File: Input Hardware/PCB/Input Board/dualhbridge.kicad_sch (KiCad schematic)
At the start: 2 parts, among them U1 DRV8837

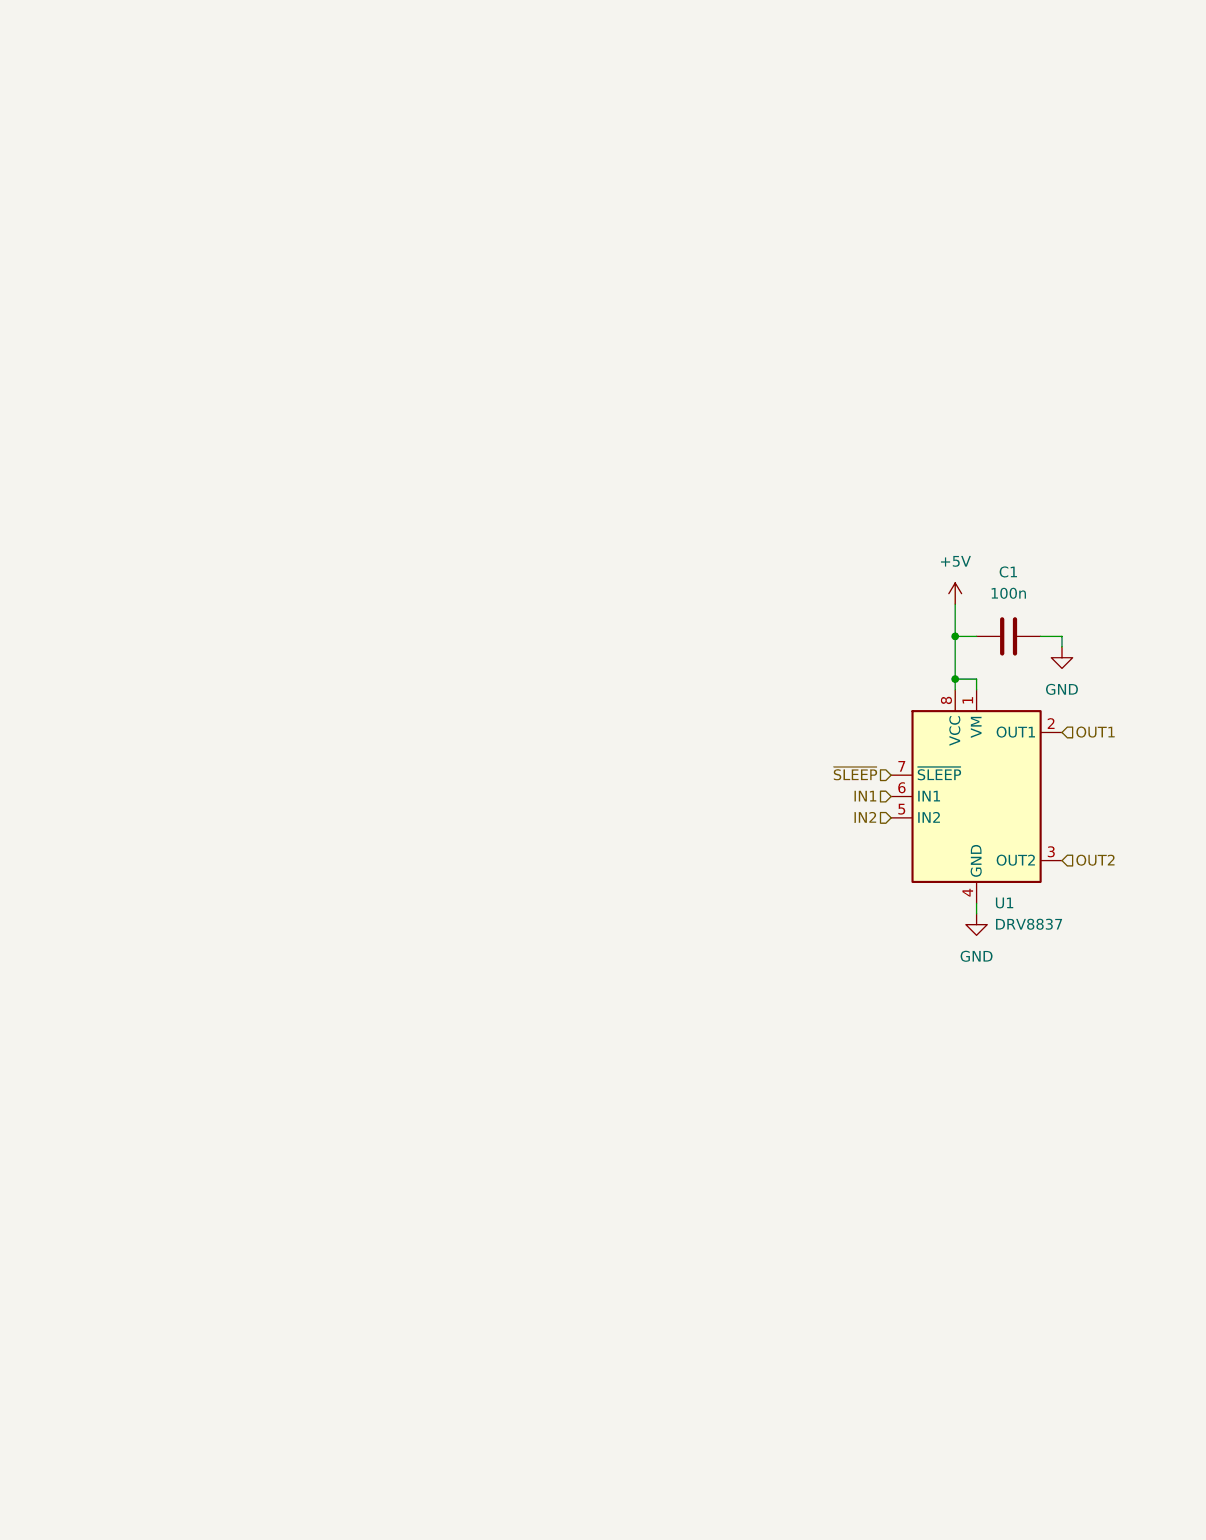
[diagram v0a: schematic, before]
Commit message: driver format update
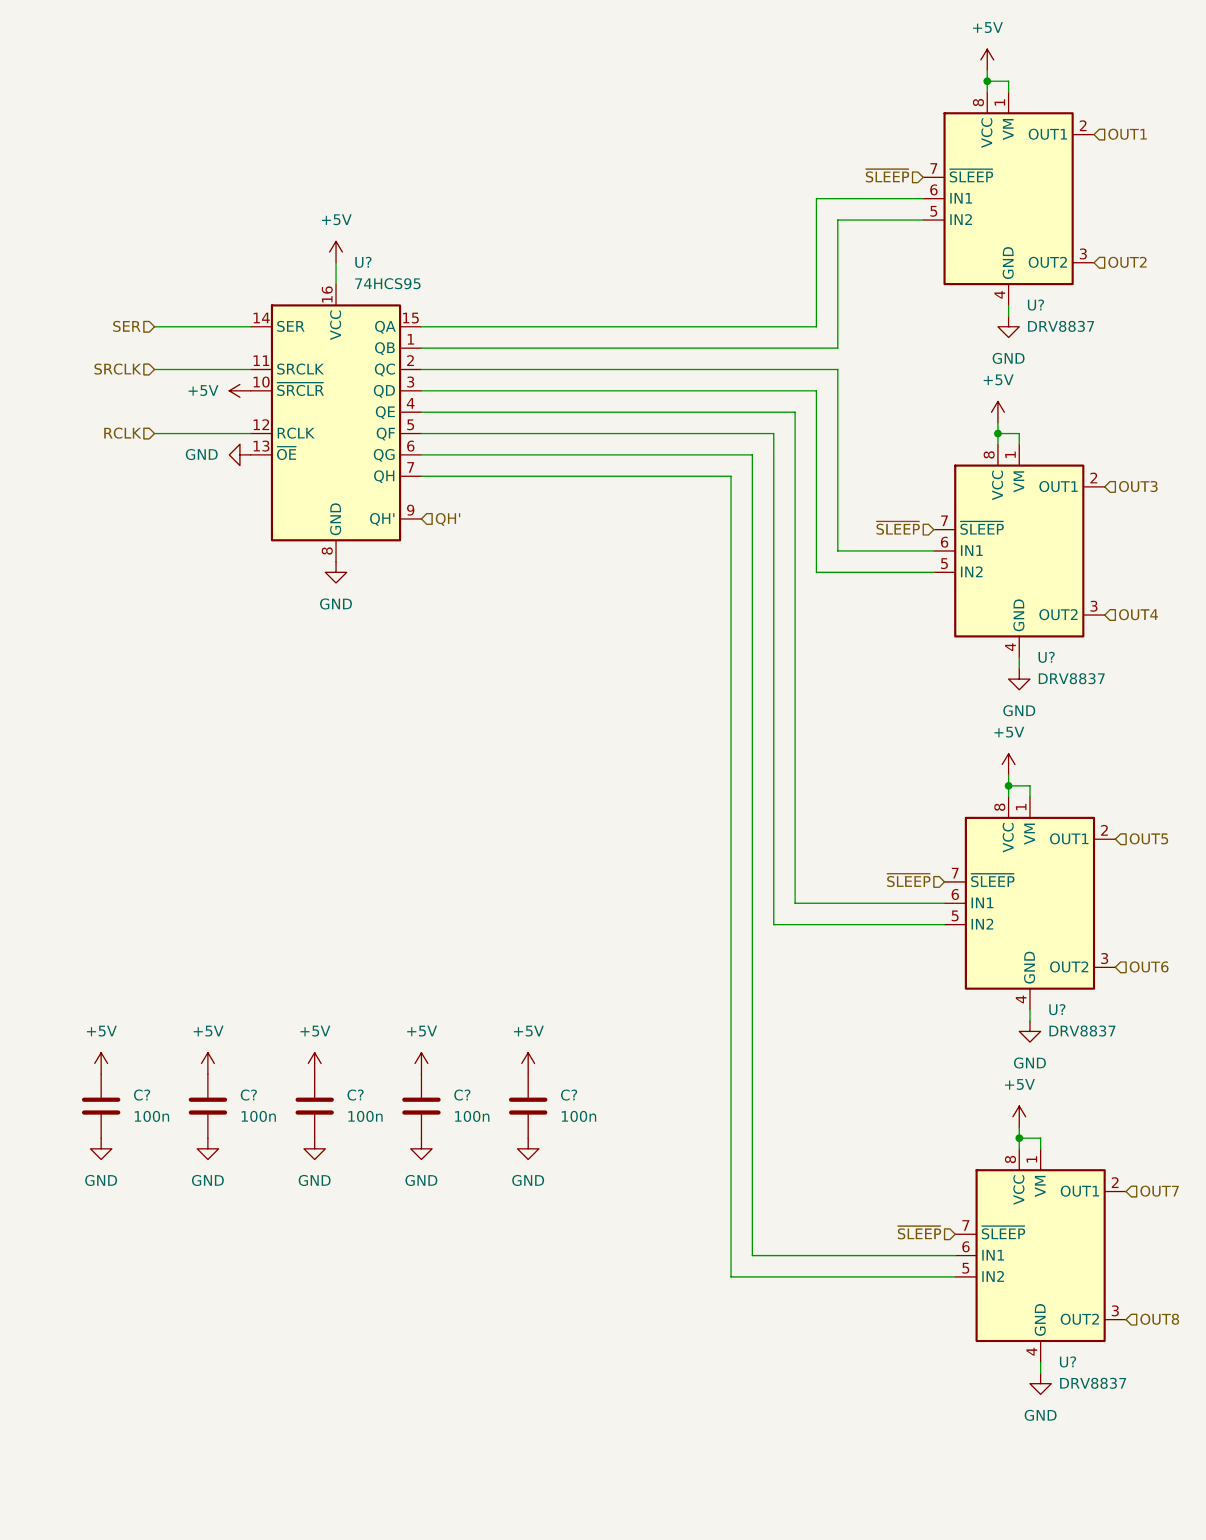
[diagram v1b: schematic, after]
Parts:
- removed C1: 100n, Capacitor_SMD:C_0603_1608Metric, symbol Device:C
- added C? (x5): 100n, Capacitor_SMD:C_0603_1608Metric, symbol Device:C
- added U? (x3): DRV8837, Package_SON:WSON-8-1EP_2x2mm_P0.5mm_EP0.9x1.6mm, symbol Driver_Motor:DRV8837
- added U?: 74HCS95, Package_SO:SOIC-16_3.9x9.9mm_P1.27mm, symbol 74xx:74HC595
- renumbered U1 to U?
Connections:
- net +5V: now also C?.2, C?.2, C?.2, C?.2, C?.2, U?.1 (VM), U?.1 (VM), U?.1 (VM), U?.10 (~{SRCLR}), U?.16 (VCC), U?.8 (VCC), U?.8 (VCC), U?.8 (VCC)
- net GND: now also C?.1, C?.1, C?.1, C?.1, C?.1, U?.13 (~{OE}), U?.4 (GND), U?.4 (GND), U?.4 (GND), U?.8 (GND), U?.9 (GND), U?.9 (GND), U?.9 (GND)
- net ~{SLEEP}: now also U?.7 (~{SLEEP}), U?.7 (~{SLEEP}), U?.7 (~{SLEEP})
- net IN1: no longer names the net of U?.6 (IN1)
- net IN1: now also U?.15 (QA)
- net IN2: no longer names the net of U?.5 (IN2)
- net IN2: now also U?.1 (QB)
- new net: U?.5 (IN2), U?.7 (QH)
- new net: U?.6 (IN1), U?.6 (QG)
- new net: U?.2 (QC), U?.6 (IN1)
- new net: U?.3 (QD), U?.5 (IN2)
- new net: U?.4 (QE), U?.6 (IN1)
- new net: U?.5 (IN2), U?.5 (QF)
- new net OUT3: U?.2 (OUT1)
- new net OUT4: U?.3 (OUT2)
- new net OUT5: U?.2 (OUT1)
- new net OUT6: U?.3 (OUT2)
- new net OUT7: U?.2 (OUT1)
- new net OUT8: U?.3 (OUT2)
- new net QH': U?.9 (QH')
- new net RCLK: U?.12 (RCLK)
- new net SER: U?.14 (SER)
- new net SRCLK: U?.11 (SRCLK)
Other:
- moved on the sheet: U?

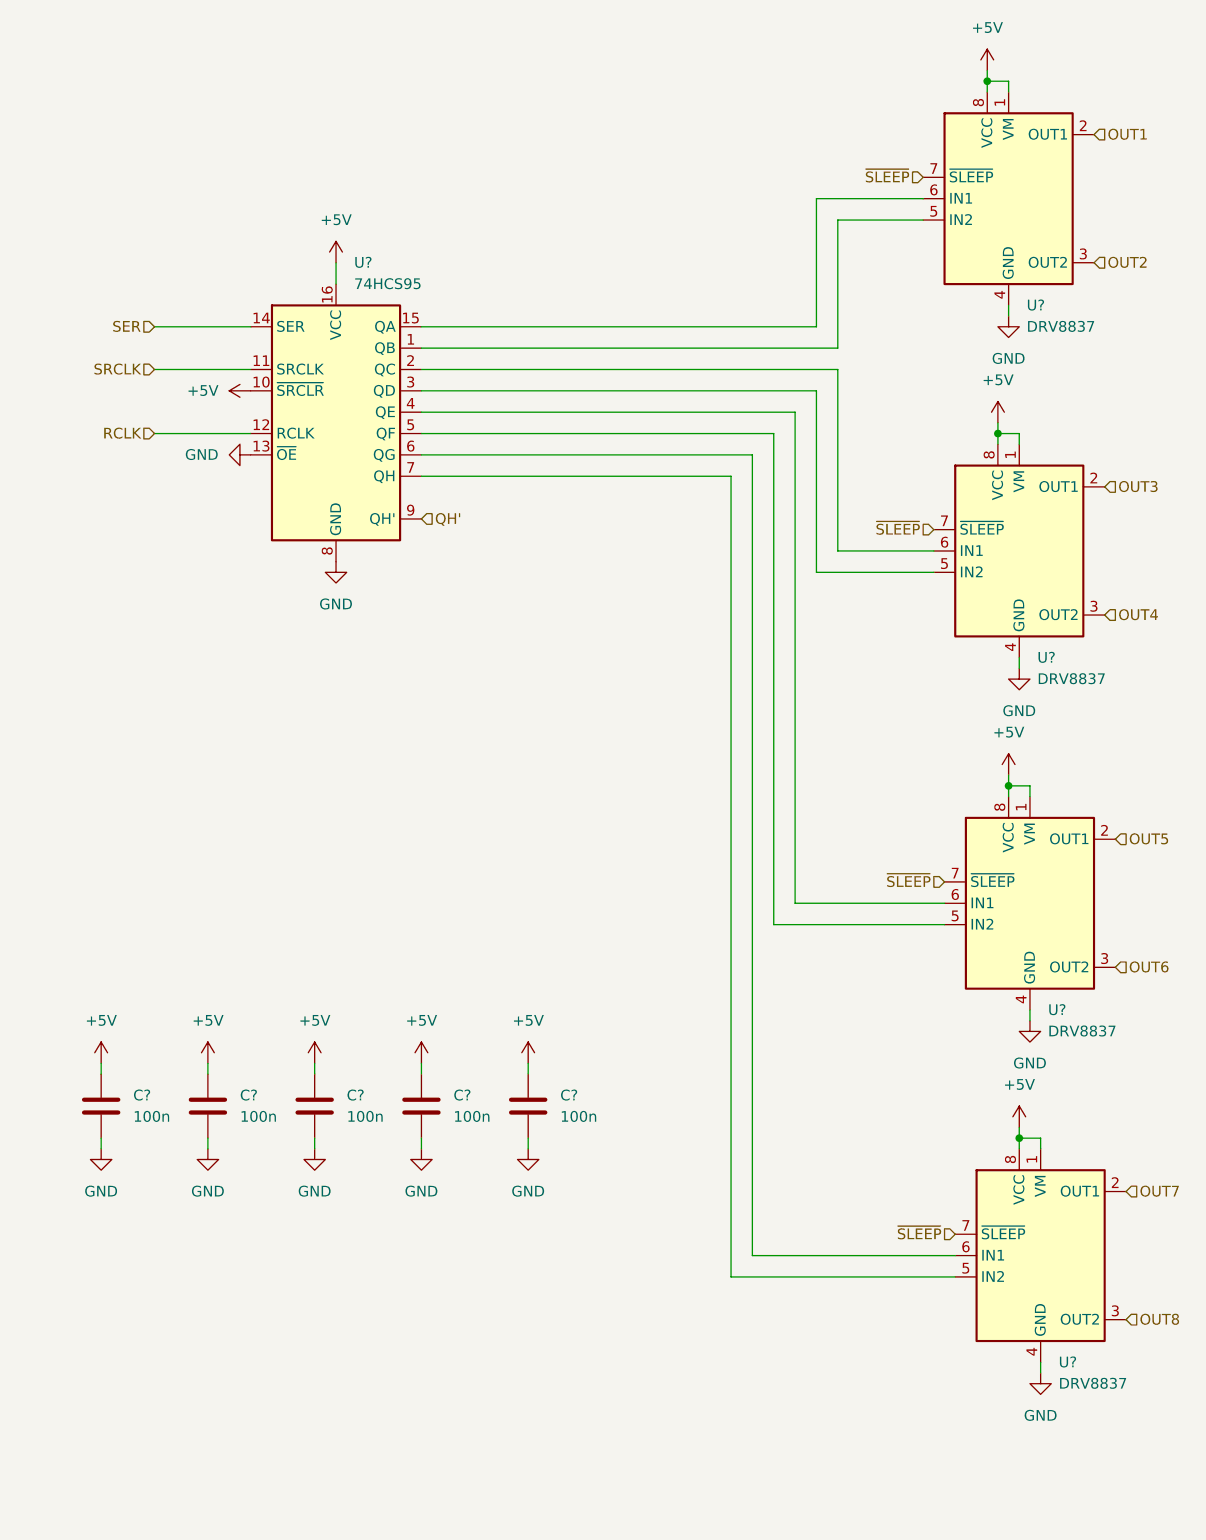
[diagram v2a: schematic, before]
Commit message: package type change
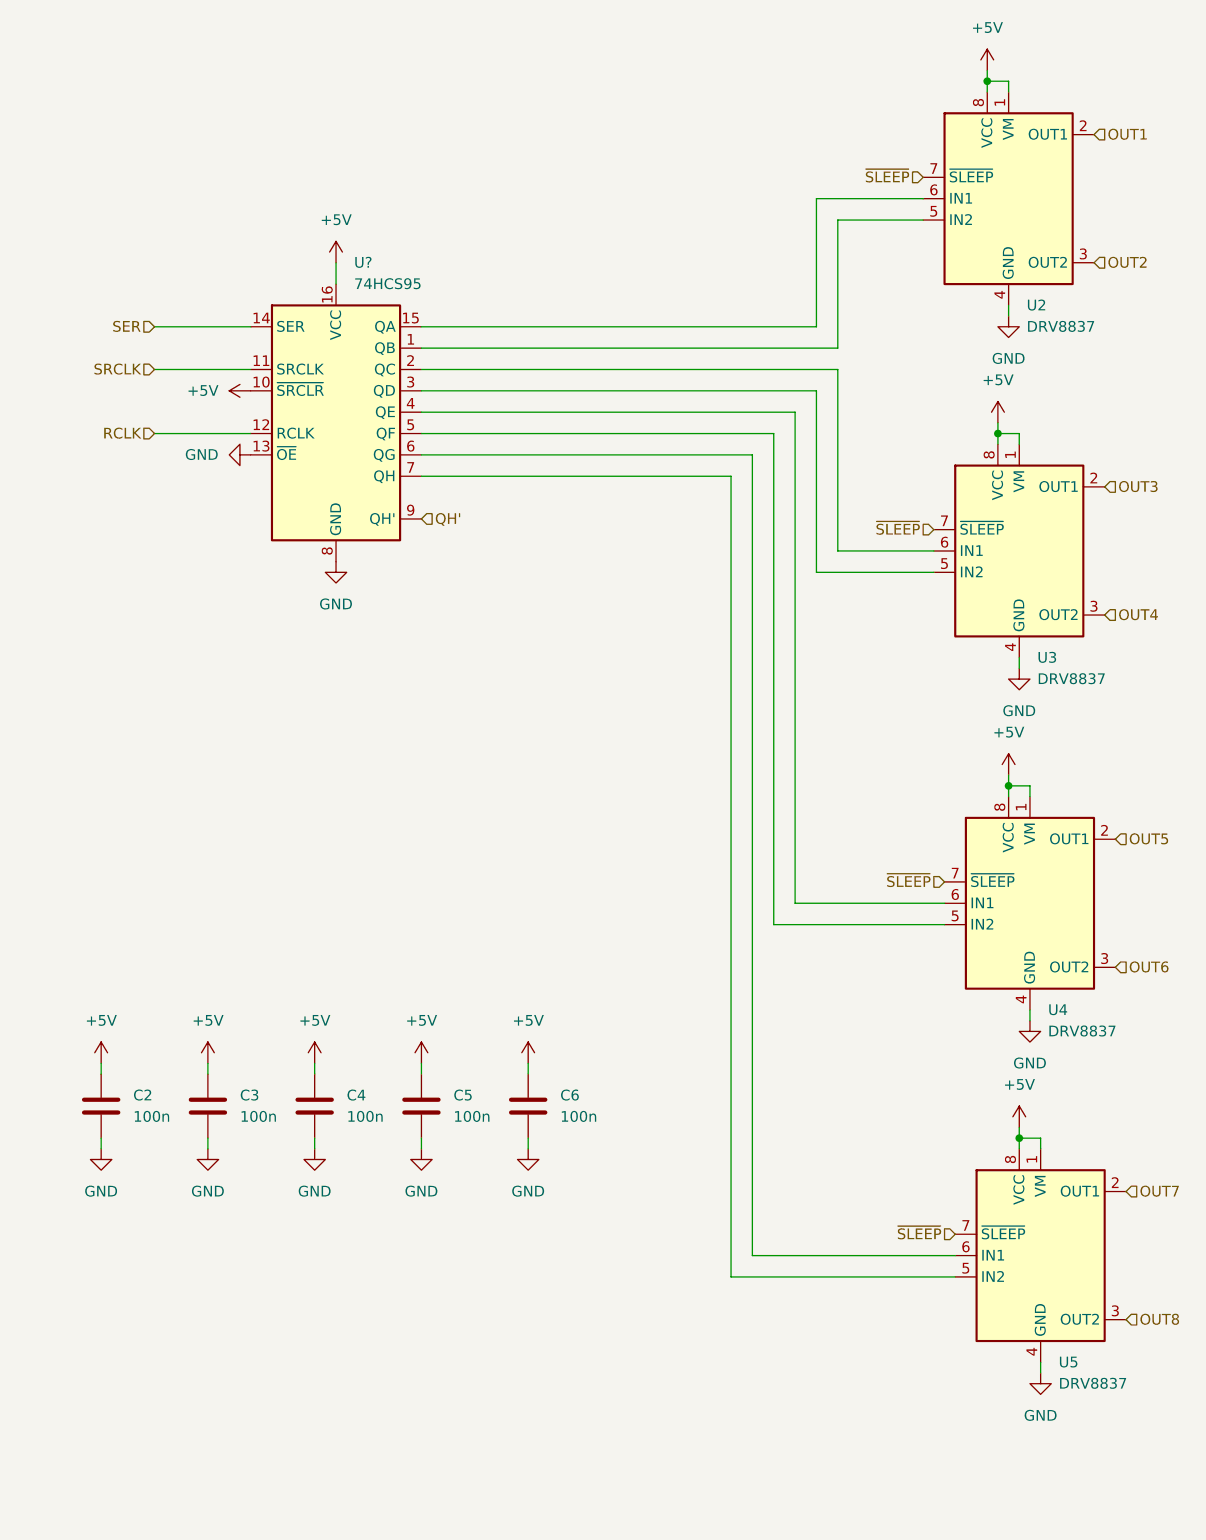
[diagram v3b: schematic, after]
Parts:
- U?: footprint Package_SO:SOIC-16_3.9x9.9mm_P1.27mm -> Package_DFN_QFN:DHVQFN-16-1EP_2.5x3.5mm_P0.5mm_EP1x2mm
- gave numbers to parts that had none: 9

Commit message: Schematic Cleanup
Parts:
- renumbered C3 to C?, C2 to C?, C5 to C?, C4 to C?, C6 to C?, U5 to U?, U2 to U?, U4 to U?, U3 to U?
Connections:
- net ~{SLEEP} is gone; now on net +5V: U?.7 (~{SLEEP}), U?.7 (~{SLEEP}), U?.7 (~{SLEEP}), U?.7 (~{SLEEP})
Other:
- moved on the sheet: C?, U?

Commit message: Layout Progress
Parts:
- gave numbers to parts that had none: 10
